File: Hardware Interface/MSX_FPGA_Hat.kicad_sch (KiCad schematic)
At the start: 24 parts, among them J1 J1, J2 J2, J3a1 J3a, J3b1 J3b, J4a1 J4a, J4b1 J4b, U1 74LVC245A, U2 74LVC245A, U3 74LVC245A, U4 74LVC245A, U5 74LVC245A

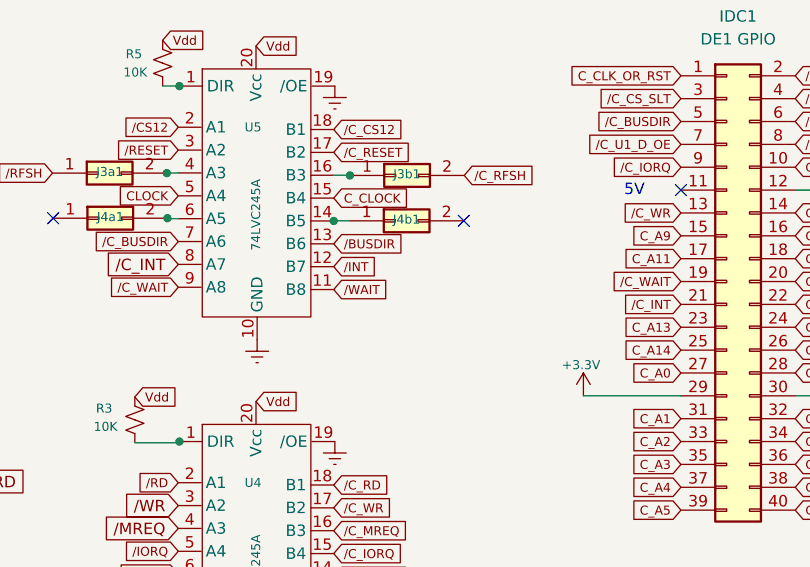
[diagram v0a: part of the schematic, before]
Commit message: Updated Add-On with silk in addresses for RPI
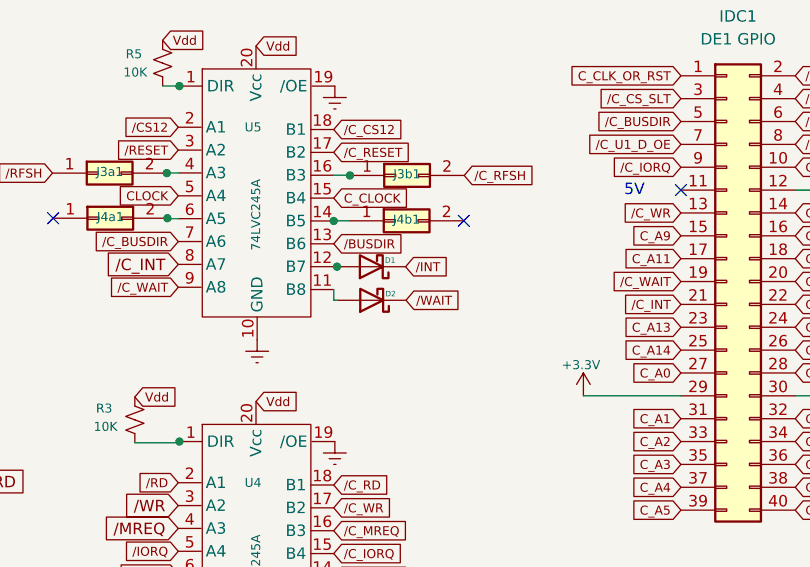
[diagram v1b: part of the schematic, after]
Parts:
- added D1, D2: BAT43, Resistor_THT:R_Axial_DIN0207_L6.3mm_D2.5mm_P7.62mm_Horizontal, symbol Device:D_Schottky
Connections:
- net /INT: now also D1.1 (K); no longer U5.12 (B7)
- net /WAIT: now also D2.1 (K); no longer U5.11 (B8)
- new net: D2.2 (A), U5.11 (B8)
- new net: D1.2 (A), U5.12 (B7)
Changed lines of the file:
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@@
   (title_block
     (title "MSX FPGA Hat")
-    (date "2023-02-17")
-    (rev "1.2")
+    (date "2023-02-20")
+    (rev "1.3")
     (company "RCC")
     (comment 1 "to 3.3v systems with voltage conversion")
@@
   )
   (junction (at 153.67 150.622) (diameter 0) (color 0 0 0 0)
+  )
+  (junction (at 90.7909 66.9333) (diameter 0) (color 0 0 0 0)
   )
   (junction (at 68.072 205.613) (diameter 0) (color 0 0 0 0)
@@
     (stroke (width 0) (type default) (color 0 0 0 0))
   )
+  (wire (pts (xy 90.424 69.469) (xy 90.424 70.6619))
+    (stroke (width 0) (type default) (color 0 0 0 0))
+  )
   (wire (pts (xy 30.353 182.245) (xy 46.228 182.245))
     (stroke (width 0) (type default) (color 0 0 0 0))
@@
     (stroke (width 0) (type default) (color 0 0 0 0))
   )
+  (wire (pts (xy 90.424 66.929) (xy 90.7909 66.929))
+    (stroke (width 0) (type default) (color 0 0 0 0))
+  )
   (wire (pts (xy 41.148 169.545) (xy 46.228 169.545))
     (stroke (width 0) (type default) (color 0 0 0 0))
@@
     (stroke (width 0) (type default) (color 0 0 0 0))
   )
+  (wire (pts (xy 90.7909 66.929) (xy 90.7909 66.9333))
+    (stroke (width 0) (type default) (color 0 0 0 0))
+  )
   (wire (pts (xy 30.353 169.545) (xy 41.148 169.545))
     (stroke (width 0) (type default) (color 0 0 0 0))
@@
   )
   (wire (pts (xy 54.864 151.511) (xy 54.864 205.613))
+    (stroke (width 0) (type default) (color 0 0 0 0))
+  )
+  (wire (pts (xy 90.424 70.6619) (xy 90.834 70.6619))
     (stroke (width 0) (type default) (color 0 0 0 0))
   )
@@
     )
   )
-  (global_label "{slash}WAIT" (shape input) (at 90.424 69.469 0) (fields_autoplaced)
-    (effects (font (size 1 1)) (justify left))
-    (property "Intersheet References" "${INTERSHEET_REFS}" (id 0) (at 96.6097 69.4065 0)
+  (global_label "{slash}WAIT" (shape input) (at 98.454 70.6619 0) (fields_autoplaced)
+    (effects (font (size 1 1)) (justify left))
+    (property "Intersheet References" "${INTERSHEET_REFS}" (id 0) (at 104.6397 70.5994 0)
       (effects (font (size 1 1)) (justify left) hide)
     )
@@
     )
   )
-  (global_label "{slash}INT" (shape input) (at 90.424 66.929 0) (fields_autoplaced)
-    (effects (font (size 1 1)) (justify left))
-    (property "Intersheet References" "${INTERSHEET_REFS}" (id 0) (at 97.0704 66.8496 0)
+  (global_label "{slash}INT" (shape input) (at 98.4109 66.9333 0) (fields_autoplaced)
+    (effects (font (size 1 1)) (justify left))
+    (property "Intersheet References" "${INTERSHEET_REFS}" (id 0) (at 105.0573 66.8539 0)
       (effects (font (size 1 1)) (justify left) hide)
     )
@@
     )
     (pin "1")
+  )
+  (symbol (lib_id "Device:D_Schottky") (at 94.644 70.6619 180) (unit 1)
+    (in_bom yes) (on_board yes)
+    (property "Reference" "D2" (id 0) (at 96.7403 69.9458 0)
+      (effects (font (size 0.6 0.6)))
+    )
+    (property "Value" "BAT43" (id 1) (at 94.9615 67.2286 0)
+      (effects (font (size 0.6 0.6)) hide)
+    )
+    (property "Footprint" "Resistor_THT:R_Axial_DIN0207_L6.3mm_D2.5mm_P7.62mm_Horizontal" (id 2) (at 94.644 70.6619 0)
+      (effects (font (size 1.27 1.27)) hide)
+    )
+    (property "Datasheet" "~" (id 3) (at 94.644 70.6619 0)
+      (effects (font (size 1.27 1.27)) hide)
+    )
+    (pin "1")
+    (pin "2")
   )
   (symbol (lib_id "power:-12V") (at 46.228 182.245 0) (unit 1)
@@
     )
     (pin "1")
+  )
+  (symbol (lib_id "Device:D_Schottky") (at 94.6009 66.9333 180) (unit 1)
+    (in_bom yes) (on_board yes)
+    (property "Reference" "D1" (id 0) (at 96.6972 66.2172 0)
+      (effects (font (size 0.6 0.6)))
+    )
+    (property "Value" "BAT43" (id 1) (at 94.9184 63.5 0)
+      (effects (font (size 0.6 0.6)) hide)
+    )
+    (property "Footprint" "Resistor_THT:R_Axial_DIN0207_L6.3mm_D2.5mm_P7.62mm_Horizontal" (id 2) (at 94.6009 66.9333 0)
+      (effects (font (size 1.27 1.27)) hide)
+    )
+    (property "Datasheet" "~" (id 3) (at 94.6009 66.9333 0)
+      (effects (font (size 1.27 1.27)) hide)
+    )
+    (pin "1")
+    (pin "2")
   )
   (symbol (lib_id "Device:C_Small") (at 147.828 153.162 0) (unit 1)
@@
       (reference "CONN1") (unit 1) (value "MSX_BUS") (footprint "Roni Footprints:MSX_CART")
     )
+    (path "/79659c5e-ee34-4dee-880c-5f7faad77490"
+      (reference "D1") (unit 1) (value "BAT43") (footprint "Resistor_THT:R_Axial_DIN0207_L6.3mm_D2.5mm_P7.62mm_Horizontal")
+    )
+    (path "/1028a945-033a-40f8-aa59-9770e8ea3db4"
+      (reference "D2") (unit 1) (value "BAT43") (footprint "Resistor_THT:R_Axial_DIN0207_L6.3mm_D2.5mm_P7.62mm_Horizontal")
+    )
     (path "/6f9656b3-3bfe-4b00-abcb-824b6a0202a0"

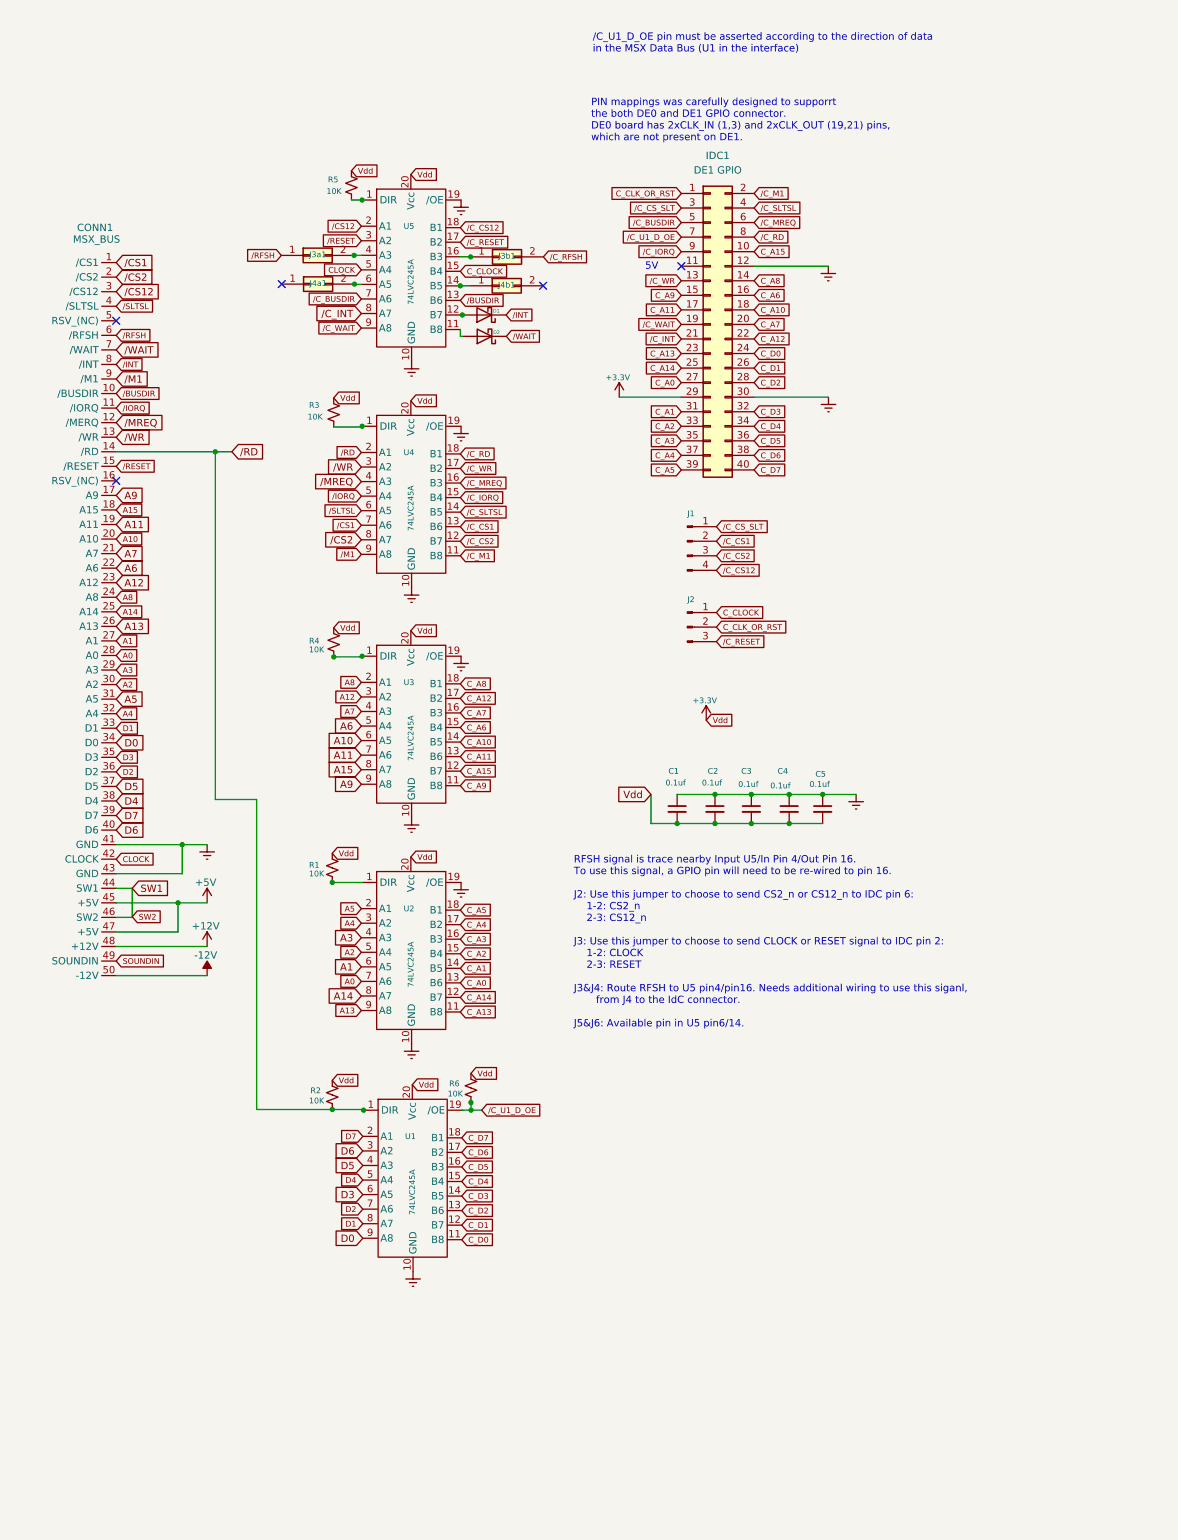
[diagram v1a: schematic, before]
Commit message: Updated schema and pcb with some cool silk and instructions
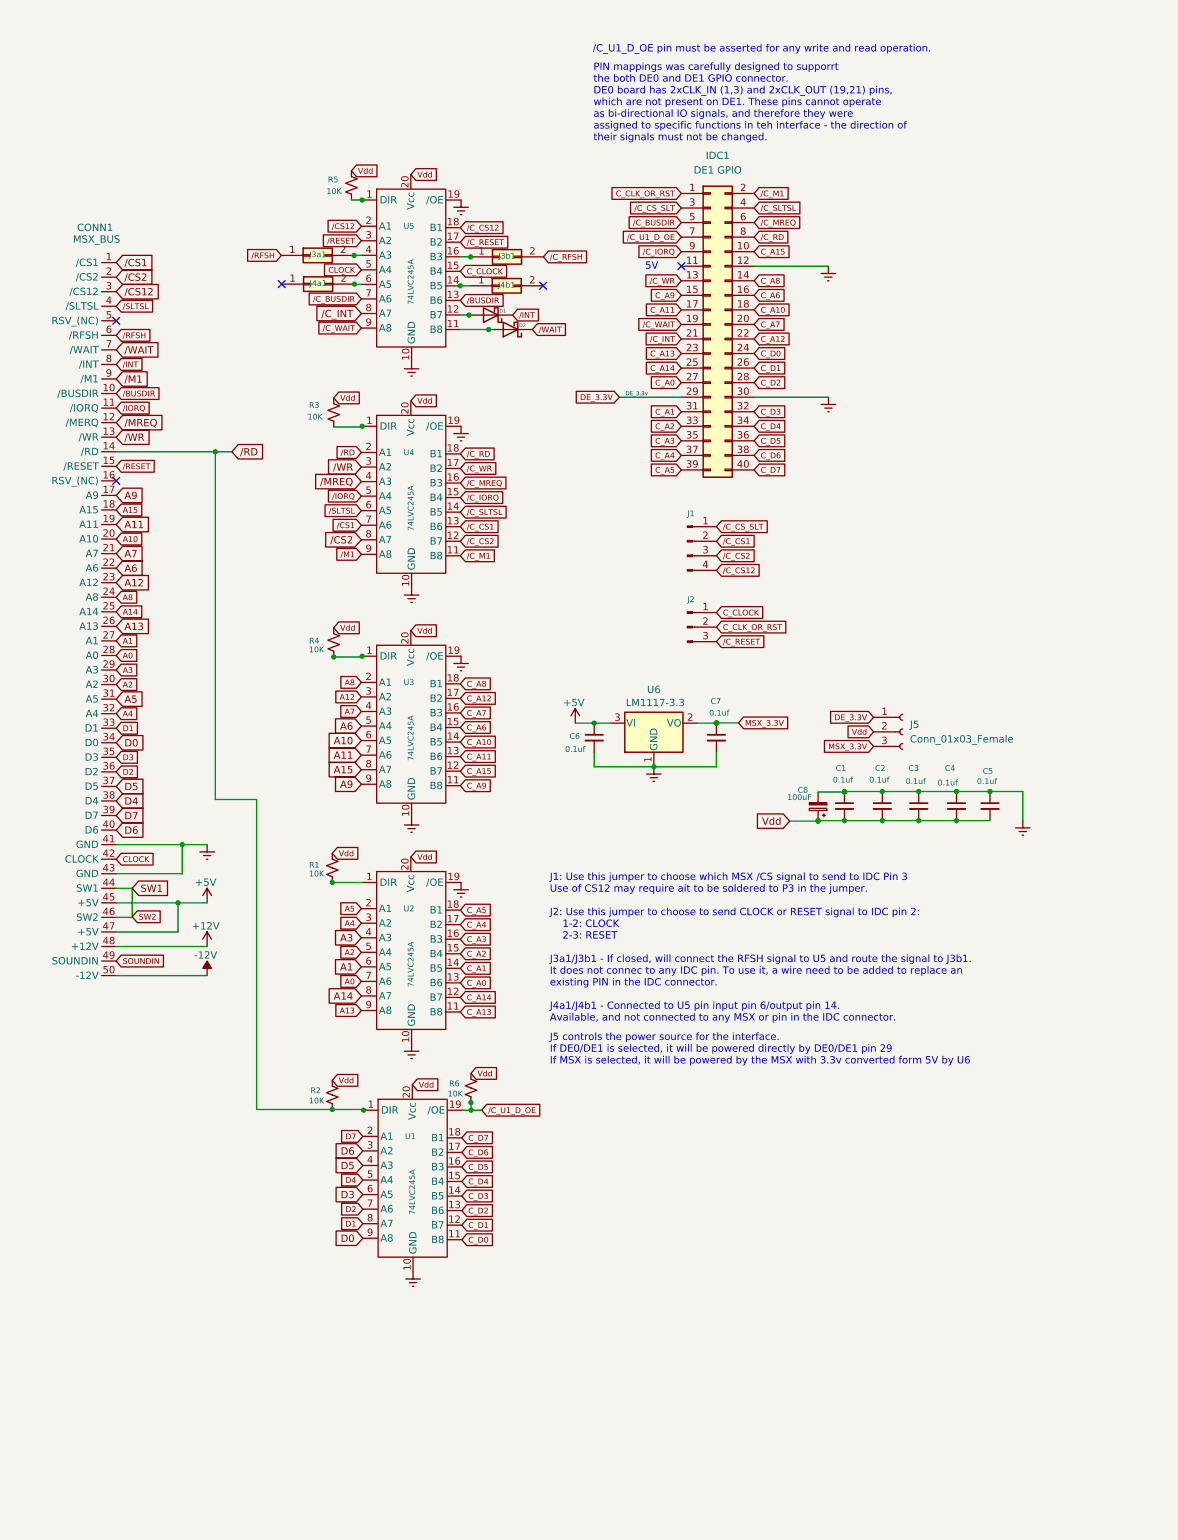
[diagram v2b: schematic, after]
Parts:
- added C6, C7: 0.1uf, Capacitor_THT:C_Disc_D3.0mm_W1.6mm_P2.50mm, symbol Device:C_Small
- added C8: 100uF, Capacitor_THT:CP_Radial_D6.3mm_P2.50mm, symbol Device:C_Polarized_Small
- added J5: Conn_01x03_Female, Connector_PinHeader_2.54mm:PinHeader_1x03_P2.54mm_Vertical, symbol Connector:Conn_01x03_Female
- added U6: LM1117-3.3, Package_TO_SOT_SMD:SOT-223-3_TabPin2, symbol Regulator_Linear:LM1117-3.3
- CONN1: footprint Roni Footprints:MSX_CART -> Roni Footprints:MSX_CART_SW
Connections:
- net +5V: now also C6.1, U6.3 (VI)
- net GNDREF: now also C6.2, C7.2, C8.2, U6.1 (GND)
- net +3.3V renamed Vdd
- net Vdd: now also C8.1, J5.2 (Pin_2); no longer IDC1.29 (Pin_29)
- new net DE_3.3V: IDC1.29 (Pin_29), J5.1 (Pin_1)
- new net MSX_3.3V: C7.1, J5.3 (Pin_3), U6.2 (VO)
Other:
- note added: "/C_U1_D_OE pin must be asserted for any write and read operation."
- note added: "J1: Use this jumper to choose which MSX /CS signal to send to IDC Pin 3 Use of CS12 may require ait to be soldered to P3 in the jumper. J2: Use this jumper to choose to send CLOCK or RESET signal to IDC pin 2: 1-2: CLOCK 2-3: RESET J3a1/J3b1 - If closed, will connect the RFSH signal to U5 and route the signal to J3b1. It does not connec to any IDC pin. To use it, a wire need to be added to replac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"
- note added: "J5 controls the power source for the interface. If DE0/DE1 is selected, it will be powered directly by DE0/DE1 pin 29 If MSX is selected, it will be powered by the MSX with 3.3v converted form 5V by U6"
- note added: "PIN mappings was carefully designed to supporrt the both DE0 and DE1 GPIO connector. DE0 board has 2xCLK_IN (1,3) and 2xCLK_OUT (19,21) pins, which are not present on DE1. These pins cannot operate as bi-directional IO signals, and therefore they were assigned to specific functions in teh interface - the direction of their signals must not be changed."
- note removed: "/C_U1_D_OE pin must be asserted according to the direction of data in the MSX Data Bus (U1 in the interface)"
- note removed: "PIN mappings was carefully designed to supporrt the both DE0 and DE1 GPIO connector. DE0 board has 2xCLK_IN (1,3) and 2xCLK_OUT (19,21) pins, which are not present on DE1."
- note removed: "RFSH signal is trace nearby Input U5/In Pin 4/Out Pin 16. To use this signal, a GPIO pin will need to be re-wired to pin 16. J2: Use this jumper to choose to send CS2_n or CS12_n to IDC pin 6: 1-2: CS2_n 2-3: CS12_n J3: Use this jumper to choose to send CLOCK or RESET signal to IDC pin 2: 1-2: CLOCK 2-3: RESET J3&J4: Route RFSH to U5 pin4/pin16. Needs additional wiring to use this siganl, from J4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"
- moved on the sheet: C1, C2, C3, C4, C5, D1, D2
